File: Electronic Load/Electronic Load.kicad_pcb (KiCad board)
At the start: 2 copper layers, 27 parts, among them J1 Load_IN, J2 Fan Connector, J3 Programming Header, J4 Load_OUT, J5 USB_C_Receptacle, Q1 IRFS3306, Q2 IRFS3306, Q3 IRFS3306, Q4 IRFS3306, SW1 Rotary_Encoder_Switch, U1 ATtiny84-20SSU, U2 MCP4551, U3 SSD1306, U4 OPA2277, U5 ACS758xCB-150U-PFF

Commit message: Updated PCB
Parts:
- added NT1: Net-Tie_2, NetTie:NetTie-2_SMD_Pad2.0mm, F.Cu at (105.0, 88.3)
- moved J5 38.8 mm to (174.0, 85.1), turned to 90 degrees
- moved U3 22.9 mm to (148.9, 46.9)
- moved J3 6.65 mm to (127.8, 89.8)
- moved R5 6.04 mm to (111.3, 88.1)
- moved R4 6.04 mm to (110.1, 89.3)
- moved U2 6.04 mm to (112.1, 84.2)
- moved U4 6.04 mm to (112.2, 84.2)
- moved C2 3.10 mm to (143.2, 71.4)
- moved C1 3.10 mm to (136.7, 71.3)
- moved R6 2.56 mm to (146.5, 71.4), turned to 270 degrees
- moved R1 2.47 mm to (137.8, 66.9), turned to 0 degrees
- moved J4 2.10 mm to (93.9, 88.1)
- moved SW1 2.10 mm to (152.5, 86.6)
- moved R2 1.84 mm to (145.3, 66.9), turned to 0 degrees
- moved R7 1.77 mm to (140.0, 71.3), turned to 90 degrees
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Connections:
- C1 pad 2: RETURN -> GND
- C2 pad 1: RETURN -> GND
- D1 pad 1: RETURN -> GND
- J3 pad 1: SCL -> MISO
- J3 pad 2: MISO -> SCL
- J3 pad 3: SDA_MOSI -> RESET
- J3 pad 4: RESET -> SDA_MOSI
- J3 pad 5: RETURN -> GND
- J5 pad A1: RETURN -> GND
- J5 pad A12: RETURN -> GND
- J5 pad B1: RETURN -> GND
- J5 pad B12: RETURN -> GND
- J5 pad S1: RETURN -> GND
- Q4 pad 3: RETURN -> GND
- R5 pad 2: RETURN -> GND
- SW1 pad C: RETURN -> GND
- SW1 pad S1: RETURN -> GND
- TH1 pad 2: RETURN -> GND
- U1 pad 14: RETURN -> GND
- U1 pad 3: Net-(U1-Pad3) -> Fan_Pin
- U1 pad 5: Fan_Pin -> Net-(U1-Pad5)
- U2 pad 4: RETURN -> GND
- U3 pad 2: RETURN -> GND
- U4 pad 4: RETURN -> GND
- U5 pad 2: RETURN -> GND
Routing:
- net RESET: track 0.00 -> 26.6 mm
- net SDA_MOSI: track 0.00 -> 25.1 mm
- net SCL: track 0.00 -> 21.7 mm
- net Fan_Pin: track 0.00 -> 21.3 mm
- net MISO: track 0.00 -> 16.2 mm
- net Enc_SW: track 0.00 -> 9.37 mm
- net Net-(J2-Pad2): track 0.00 -> 8.84 mm
- net +5V: track 0.00 -> 7.49 mm
- net Net-(R3-Pad1): track 0.00 -> 4.33 mm
- net Net-(D1-Pad2): track 0.00 -> 1.94 mm
- added copper zone on B.Cu, net GND
- added copper zone on F.Cu, net GND
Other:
- board outline added: 92.5 x 53.6 mm

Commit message: Updated PCB
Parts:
- added C3: 10uF, Capacitor_SMD:CP_Elec_4x5.4, F.Cu at (164.2, 88.1)
- C1, C2, R1, R2, R4, R6, R7, U2: moved to F.Cu
- moved R4 12.8 mm to (122.9, 90.2), turned to 270 degrees
- moved J3 8.41 mm to (133.8, 83.9)
- moved R5 8.13 mm to (118.9, 91.0), turned to 180 degrees
- moved U2 6.86 mm to (118.0, 87.7), turned to 0 degrees
- moved U4 3.50 mm to (112.3, 87.7)
- moved C2 0.10 mm to (143.2, 71.3)
- moved R6 0.10 mm to (146.5, 71.3)
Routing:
- net SDA_MOSI: track 25.1 -> 77.0 mm, vias 0 -> 1
- net SCL: track 21.7 -> 66.6 mm, vias 0 -> 1
- net Gate: track 0.00 -> 43.7 mm, vias 0 -> 2
- net Tout: track 0.00 -> 36.8 mm
- net Net-(R1-Pad2): track 0.00 -> 28.5 mm, vias 0 -> 2
- net Net-(R2-Pad2): track 0.00 -> 24.0 mm, vias 0 -> 2
- net Vout: track 0.00 -> 23.4 mm, vias 0 -> 2
- net EncB: track 0.00 -> 13.2 mm
- net GND: track 0.00 -> 12.2 mm
- net RESET: track 26.6 -> 14.6 mm
- net +5V: track 7.49 -> 18.1 mm
- net MISO: track 16.2 -> 6.10 mm
- net EncA: track 0.00 -> 6.25 mm
- net Fan_Pin: track 21.3 -> 20.4 mm
- added copper zone on F.Cu, net +5V
- added copper zone on F.Cu, net Net-(J1-Pad1)
- added copper zone on F.Cu, net Net-(Q1-Pad2)
- added copper zone on F.Cu, net RETURN
- removed copper zone on F.Cu, net GND

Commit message: Updated PCB and code
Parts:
- added C4: 1uF, Capacitor_SMD:C_1206_3216Metric, F.Cu at (108.0, 93.1)
- added C5: 10uF, Capacitor_SMD:CP_Elec_4x5.4, F.Cu at (164.1, 88.0)
- added C6: 1uF, Capacitor_SMD:C_1206_3216Metric, F.Cu at (129.6, 90.6)
- added C7: 1uF, Capacitor_SMD:C_1206_3216Metric, F.Cu at (128.5, 49.4)
- C3: value 10uF -> 1uF; footprint Capacitor_SMD:CP_Elec_4x5.4 -> Capacitor_SMD:C_1206_3216Metric
- U4: value OPA2277 -> OPA277
- moved C3 44.2 mm to (125.8, 66.3), turned to 90 degrees
- moved U2 5.66 mm to (121.3, 92.3), turned to 180 degrees
- moved R7 4.65 mm to (114.7, 93.0)
- moved R6 4.12 mm to (119.1, 88.6), turned to 180 degrees
- moved R3 3.30 mm to (143.3, 71.3)
- moved C2 3.20 mm to (140.0, 71.3)
- moved R8 2.88 mm to (123.0, 62.6)
- moved U4 2.06 mm to (111.3, 89.5), turned to 180 degrees
- moved R2 1.90 mm to (143.4, 66.9)
- moved R5 1.00 mm to (125.5, 72.9)
- moved D1 0.91 mm to (124.4, 76.8), turned to 0 degrees
- renumbered J3 to J1, J1 to J2, J4 to J3, J5 to J4, J2 to J5, R7 to R3, R6 to R4, R3 to R5, R4 to R6, R5 to R7, U5 to U6
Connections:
- net Net-(J1-Pad1) renamed /Load_In
- net Net-(Q1-Pad2) renamed /MOSFET_Drain
- net Net-(R1-Pad2) renamed /A
- net Net-(R2-Pad2) renamed /B
- C3 pad 1: +5V -> GND
- C3 pad 2: GND -> +5V
- U1 pad 10: Enc_SW -> Net-(U1-Pad10)
- U1 pad 5: Net-(U1-Pad5) -> Enc_SW
- U4 pad 1: Gate -> Net-(U4-Pad1)
- U4 pad 5: (no net) -> Net-(U4-Pad5)
- U4 pad 6: (no net) -> Gate
- U4 pad 7: (no net) -> +5V
- U4 pad 8: +5V -> Net-(U4-Pad8)
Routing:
- net +5V: track 18.1 -> 223.0 mm, vias 0 -> 2
- net Vout: track 23.4 -> 62.2 mm, vias 2 -> 3
- net GND: track 12.2 -> 31.1 mm, vias 0 -> 33
- net SCL: track 66.6 -> 80.2 mm, vias 1 -> 2
- net SDA_MOSI: track 77.0 -> 87.1 mm, vias 1 -> 2
- net Net-(U2-Pad6): track 0.00 -> 7.50 mm
- net EncA: track 6.25 -> 11.4 mm
- net Tout: track 36.8 -> 31.9 mm
- net RETURN: track 0.00 -> 4.75 mm
- net /B: track 24.0 -> 19.7 mm, vias 2 -> 1
- net Net-(R6-Pad2): track 0.00 -> 3.35 mm
- net Net-(R7-Pad1): track 0.00 -> 3.14 mm
- net Enc_SW: track 9.37 -> 11.8 mm, vias 0 -> 1
- net Gate: track 43.7 -> 46.0 mm
- net RESET: track 14.6 -> 16.9 mm
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- added copper zone on F.Cu, net GND
- removed copper zone on F.Cu, net +5V

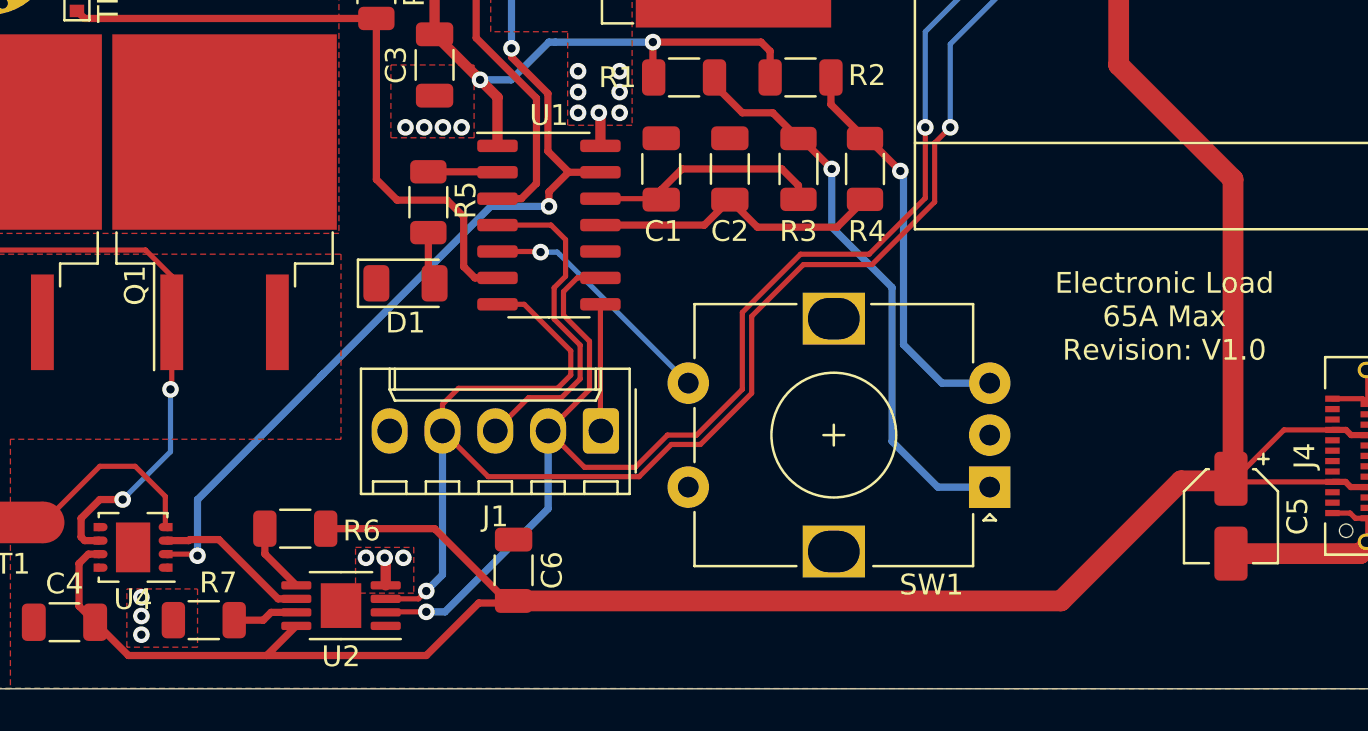
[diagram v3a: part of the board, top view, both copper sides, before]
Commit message: Updated PCB
Added potentiometers instead of fixed resistors on R6 and R7. Allows accurate changing of resistance to get good current ranges
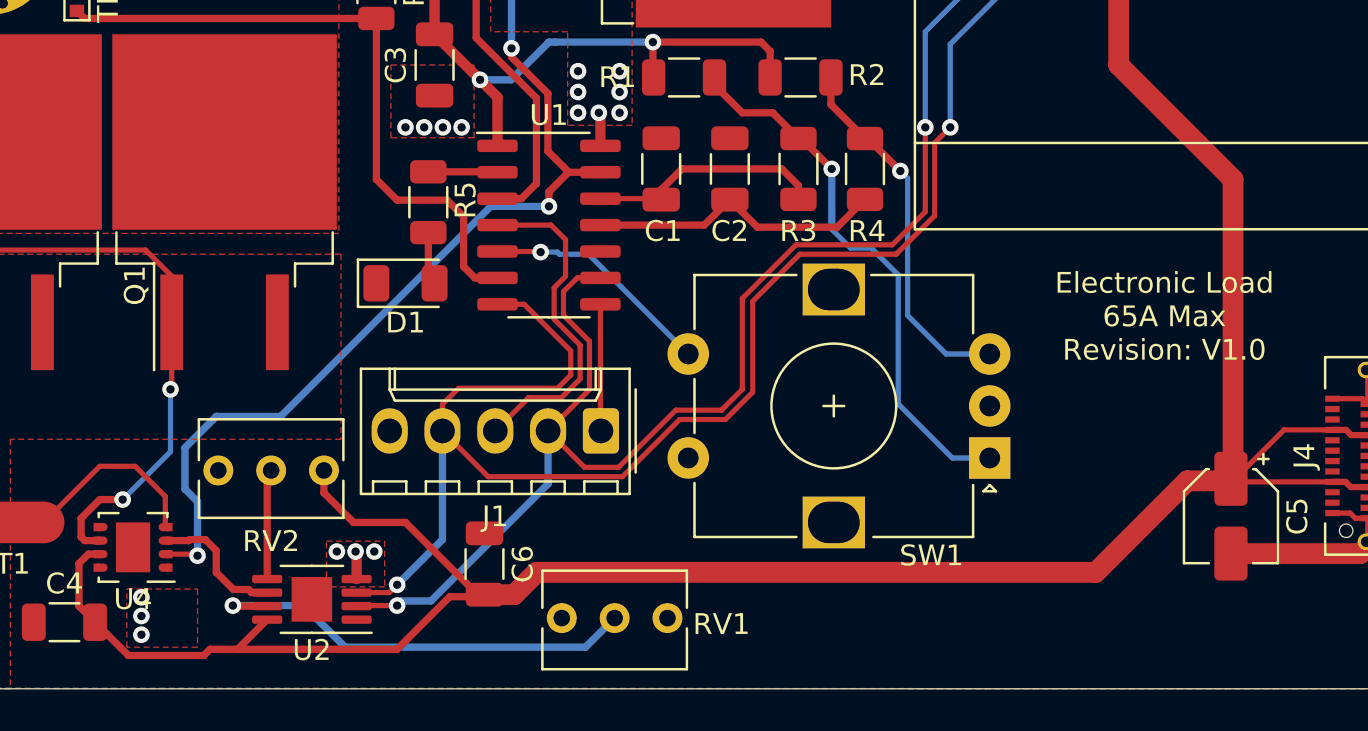
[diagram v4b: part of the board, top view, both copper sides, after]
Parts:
- removed R6, R7: R, Resistor_SMD:R_1206_3216Metric
- added RV1: R_POT, Potentiometer_THT:Potentiometer_Bourns_3266Y_Vertical, F.Cu at (137.0, 92.9)
- added RV2: R_POT, Potentiometer_THT:Potentiometer_Bourns_3266Y_Vertical, F.Cu at (115.4, 85.8)
- moved C6 1.43 mm to (128.2, 90.3)
- moved U2 1.43 mm to (119.9, 92.0)
- moved SW1 1.40 mm to (152.5, 85.2)
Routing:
- net Net-(RV1-Pad2): track 3.14 -> 21.4 mm, vias 0 -> 1
- net Vout: track 62.2 -> 56.0 mm
- net Net-(RV2-Pad2): track 3.35 -> 5.30 mm
- net SCL: track 80.2 -> 81.6 mm
- net /B: track 19.7 -> 18.4 mm
- net /A: track 27.6 -> 26.4 mm
- net SDA_MOSI: track 87.1 -> 88.2 mm
- net Net-(U2-Pad6): track 7.50 -> 6.59 mm
- net Enc_SW: track 11.8 -> 11.3 mm

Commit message: update
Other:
- net class Default removed
